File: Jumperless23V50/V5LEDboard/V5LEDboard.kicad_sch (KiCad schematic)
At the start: 48 parts

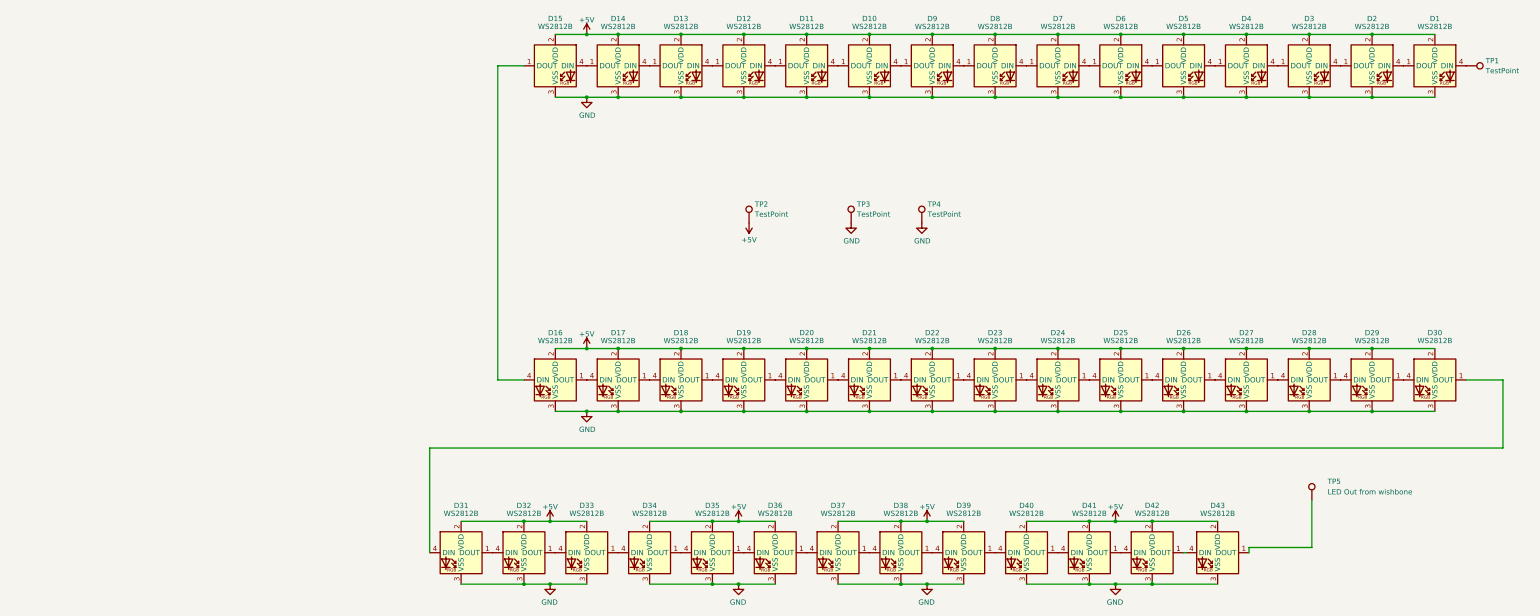
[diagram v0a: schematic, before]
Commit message: made a schematic with everything on one sheet
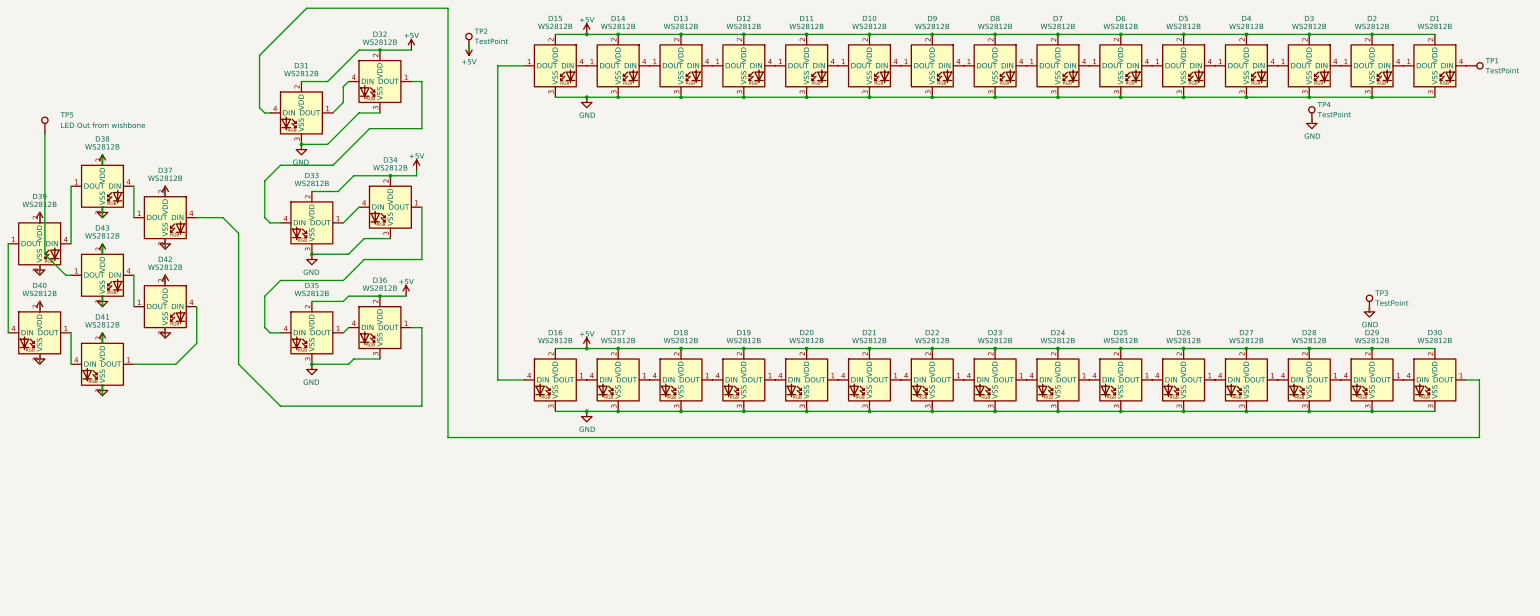
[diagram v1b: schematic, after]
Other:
- moved on the sheet: D31, D32, D33, D34, D35, D36, D37, D38, D39, D40, D41, D42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
